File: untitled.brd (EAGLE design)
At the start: 59.4 x 57.8 mm, 21 parts

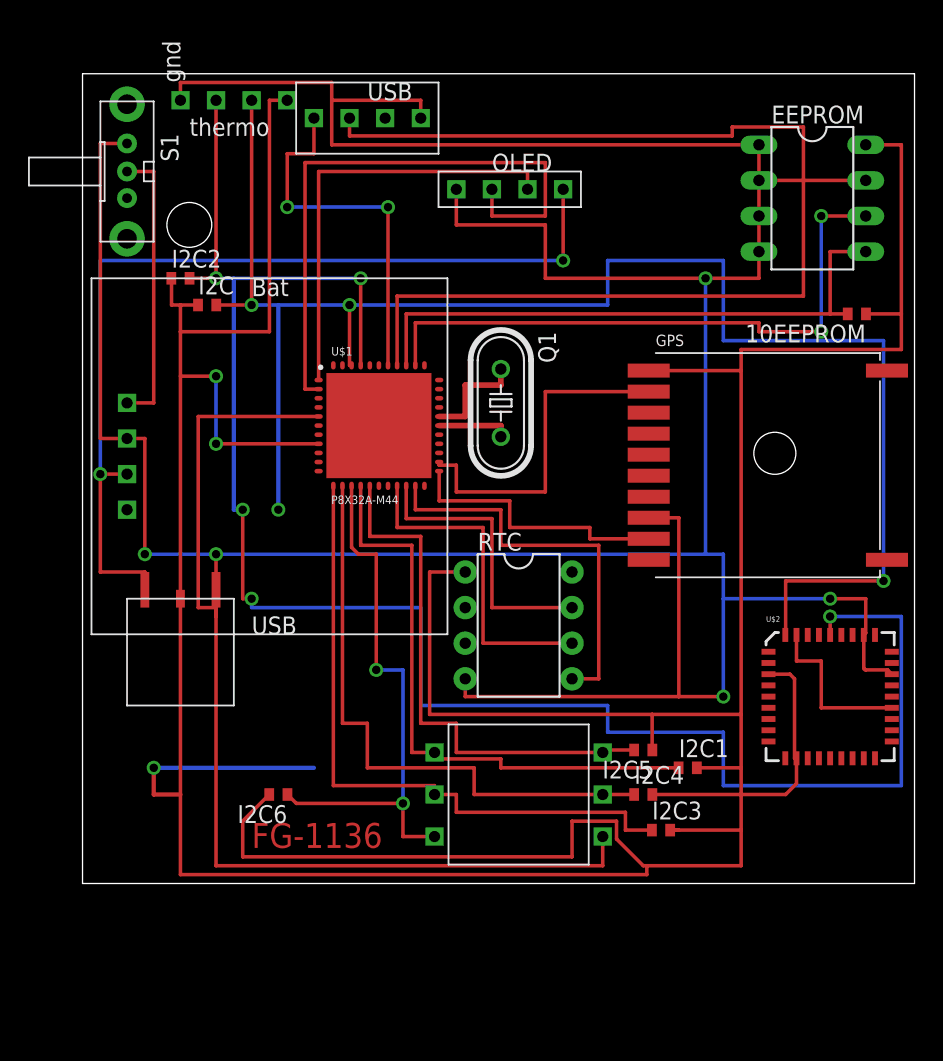
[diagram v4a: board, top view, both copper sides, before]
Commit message: Board cleanup
* Removed traces to nowhere
* Made all vias round
* Optimized some traces to remove vias
* Made better connections to SMT pads
* Connected missing ground on compass
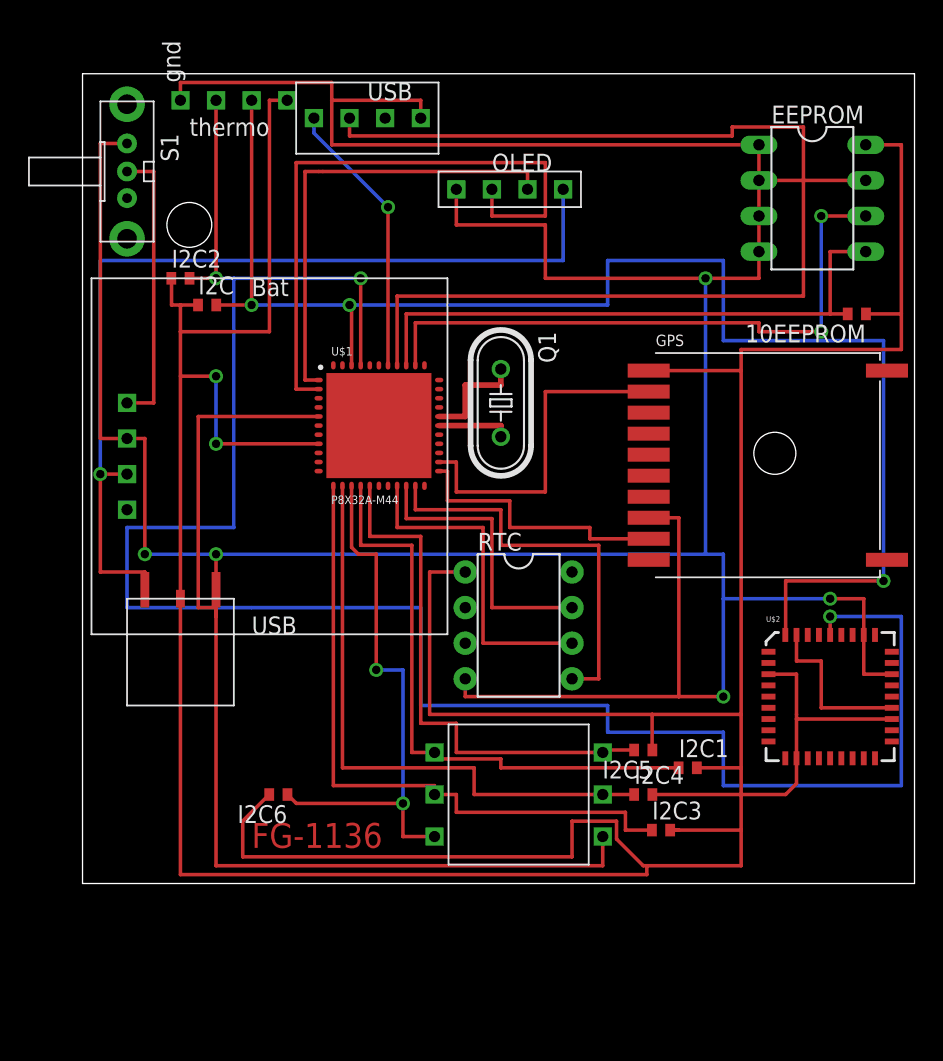
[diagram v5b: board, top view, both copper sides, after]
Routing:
- net SCL: track 133.4 -> 148.6 mm, vias 5 -> 3
- net SDA: track 118.2 -> 103.5 mm, vias 4 -> 3
- net VCC: track 303.6 -> 295.3 mm, vias 1 -> 0
- net N$7: track 26.7 -> 19.8 mm, vias 2 -> 1
- net N$11: track 31.1 -> 33.0 mm
- net N$10: track 43.8 -> 45.1 mm
- net N$12: vias 2 -> 1

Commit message: Add supply symbols, didn't fix board
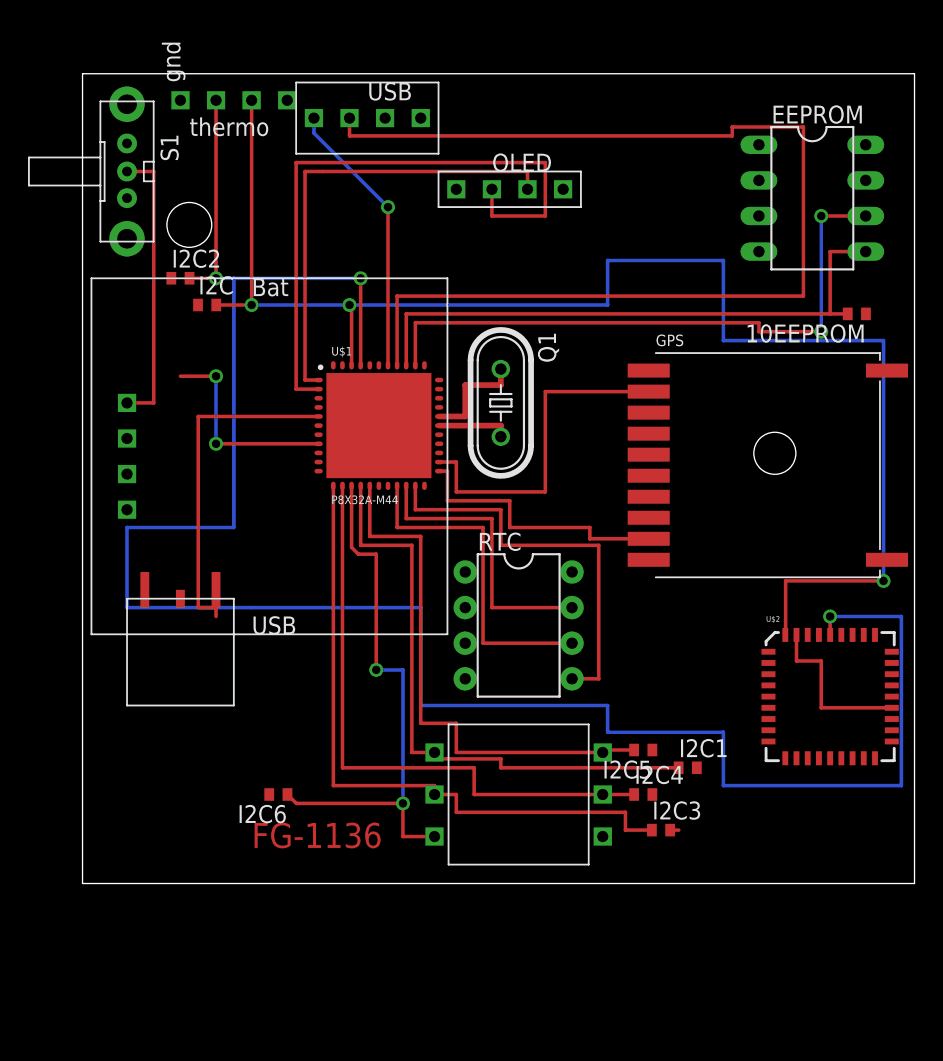
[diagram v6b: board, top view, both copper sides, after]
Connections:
- net N$12 renamed +5V
- removed net VCC: 10EEPROM.1, EEPROM.8, GPS.P$1, I2C.1, I2C1.2, I2C2.1, I2C3.2, I2C4.2, I2C5.1, I2C6.2, RTC.1, THERMO.VCC, U$2.11, U$2.21, U$2.3
- new net +3V3: 10EEPROM.1, 3.3LDO.VOUT, EEPROM.8, I2C.1, I2C1.2, I2C2.1, I2C3.2, I2C4.2, I2C5.1, I2C6.2, RTC.1, THERMO.VCC, U$2.11, U$2.21, U$2.3
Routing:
- net GND: track 309.1 -> 0.00 mm, vias 5 -> 0
- net VCC: track 295.3 -> 0.00 mm
- net +5V: track 66.0 -> 0.00 mm, vias 1 -> 0

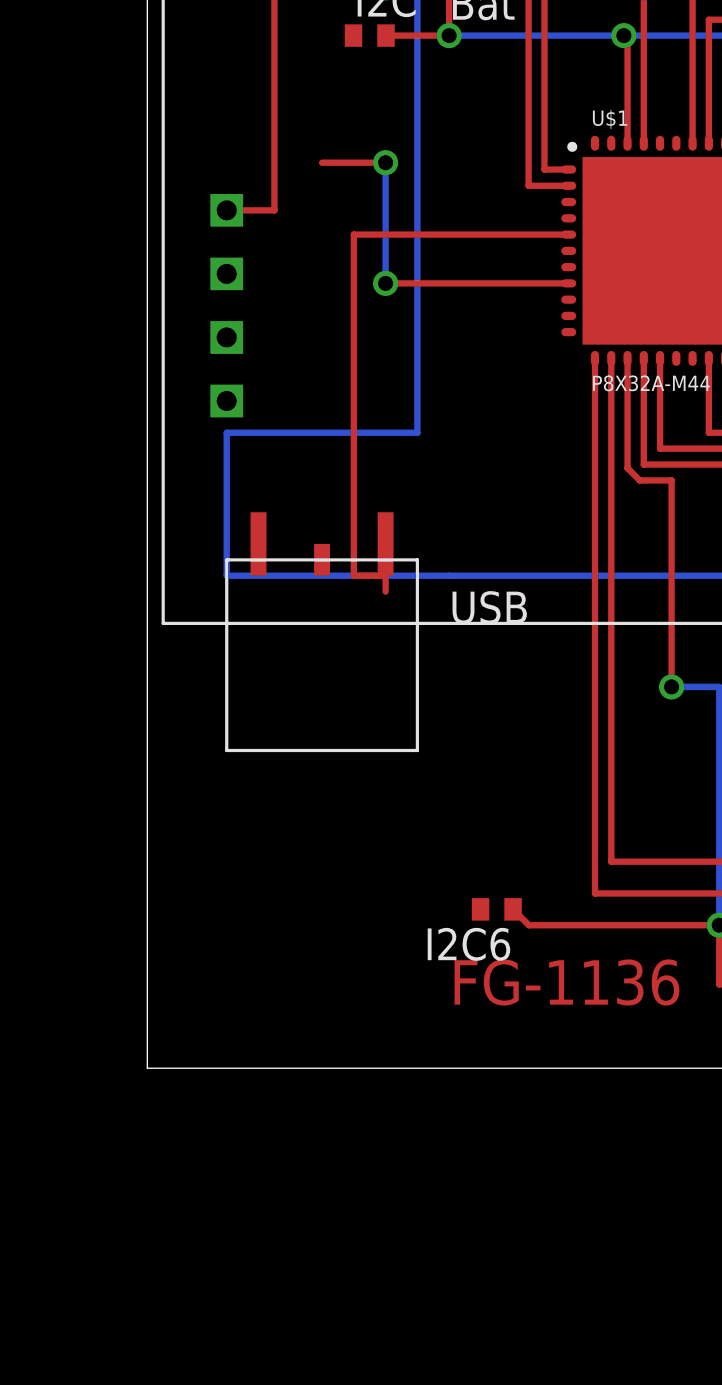
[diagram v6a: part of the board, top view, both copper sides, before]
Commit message: Added power and decoupling caps to schematic
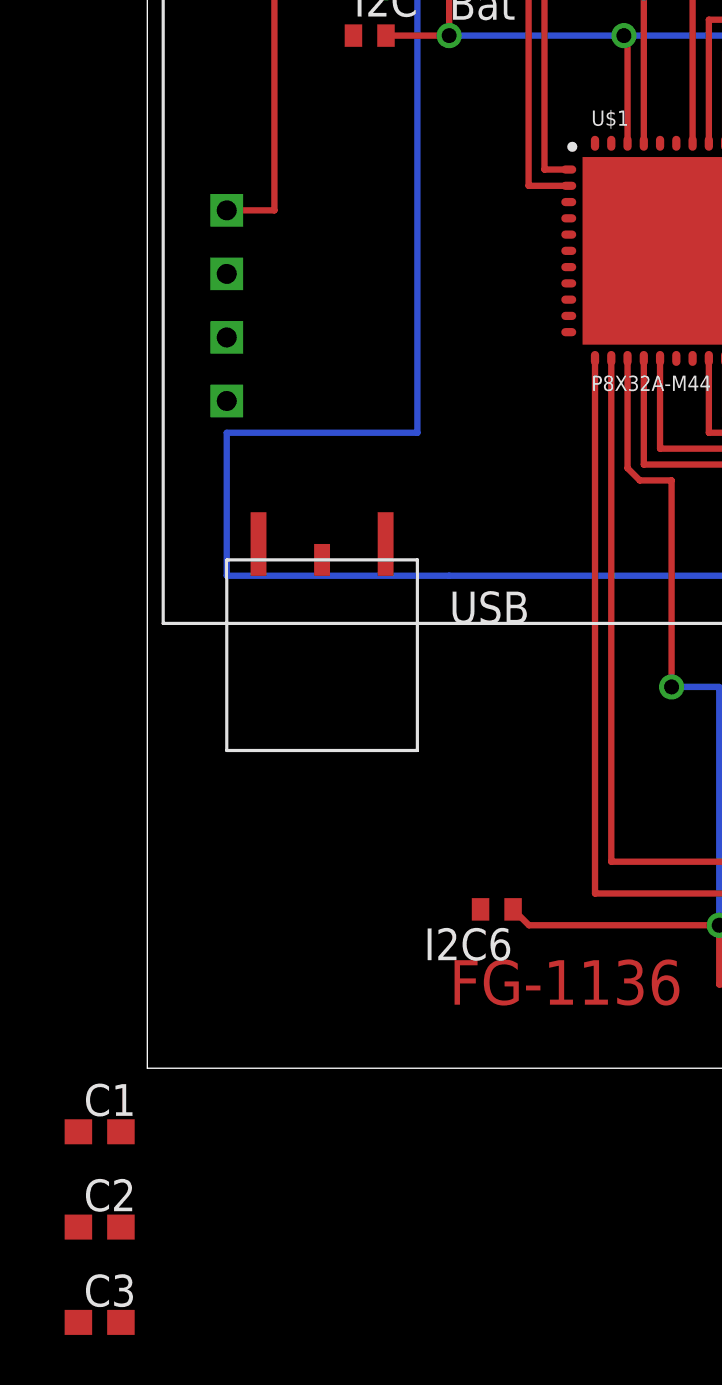
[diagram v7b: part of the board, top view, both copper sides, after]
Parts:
- added C1, C2, C3: (no value), rcl:C0603
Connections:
- removed net VDD: U$1.18, U$1.30, U$1.40, U$1.8
- removed net VSS: U$1.17, U$1.27, U$1.39, U$1.5
- net +3V3: now also C1.1, C2.1, C3.1, U$1.18, U$1.30, U$1.40, U$1.8
- net GND: now also C1.2, C2.2, C3.2, U$1.17, U$1.27, U$1.39, U$1.5
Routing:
- net VSS: track 24.1 -> 0.00 mm
- net VDD: track 14.7 -> 0.00 mm, vias 2 -> 0
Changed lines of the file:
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@@
 <element name="I2C1" library="adafruit" package="R1005" value="" x="76.835" y="18.415"/>
 <element name="U$2" library="SparkFun" package="LCC36" value="HMC6343A" x="86.995" y="23.495"/>
+<element name="C1" library="rcl" package="C0603" value="" x="31.75" y="7.62"/>
+<element name="C2" library="rcl" package="C0603" value="" x="31.75" y="3.81"/>
+<element name="C3" library="rcl" package="C0603" value="" x="31.75" y="0"/>
 </elements>
 <signals>
-<signal name="VDD">
-<contactref element="U$1" pad="8"/>
-<contactref element="U$1" pad="18"/>
-<contactref element="U$1" pad="30"/>
-<contactref element="U$1" pad="40"/>
-<wire x1="50.5" y1="41.5313" x2="43.18" y2="41.5313" width="0.254" layer="1"/>
-<wire x1="43.18" y1="41.5313" x2="43.18" y2="46.355" width="0.254" layer="16"/>
-<wire x1="43.18" y1="46.355" x2="40.64" y2="46.355" width="0.254" layer="1"/>
-<via x="43.18" y="41.5313" extent="1-16" drill="0.6"/>
-<via x="43.18" y="46.355" extent="1-16" drill="0.6"/>
-<wire x1="54.15" y1="47.1313" x2="59.1" y2="44.1313" width="0" layer="19" extent="1-1"/>
-<wire x1="55.45" y1="38.5313" x2="59.1" y2="44.1313" width="0" layer="19" extent="1-1"/>
-<wire x1="50.5" y1="41.5313" x2="55.45" y2="38.5313" width="0" layer="19" extent="1-1"/>
-</signal>
-<signal name="VSS">
-<contactref element="U$1" pad="5"/>
-<contactref element="U$1" pad="17"/>
-<contactref element="U$1" pad="27"/>
-<contactref element="U$1" pad="39"/>
-<wire x1="50.5" y1="43.4813" x2="41.91" y2="43.4813" width="0.254" layer="1"/>
-<wire x1="41.91" y1="43.4813" x2="41.91" y2="29.845" width="0.254" layer="1"/>
-<wire x1="41.91" y1="29.845" x2="43.18" y2="29.845" width="0.254" layer="1"/>
-<wire x1="43.18" y1="29.845" x2="43.18" y2="29.21" width="0.254" layer="1"/>
-<wire x1="54.8" y1="38.5313" x2="59.1" y2="42.1813" width="0" layer="19" extent="1-1"/>
-<wire x1="54.8" y1="47.1313" x2="59.1" y2="42.1813" width="0" layer="19" extent="1-1"/>
-<wire x1="50.5" y1="43.4813" x2="54.8" y2="47.1313" width="0" layer="19" extent="1-1"/>
-</signal>
 <signal name="VBAT">
 <contactref element="RTC" pad="8"/>
@@
 <contactref element="U$2" pad="29"/>
 <contactref element="THERMO" pad="GND"/>
+<contactref element="U$1" pad="39"/>
+<contactref element="U$1" pad="27"/>
+<contactref element="U$1" pad="17"/>
+<contactref element="U$1" pad="5"/>
+<contactref element="C2" pad="2"/>
+<contactref element="C1" pad="2"/>
+<contactref element="C3" pad="2"/>
 <wire x1="81.915" y1="60.325" x2="89.535" y2="60.325" width="0" layer="19" extent="1-1"/>
 <wire x1="81.915" y1="62.865" x2="81.915" y2="60.325" width="0" layer="19" extent="1-1"/>
@@
 <wire x1="81.915" y1="55.245" x2="81.915" y2="57.785" width="0" layer="19" extent="1-1"/>
 <wire x1="74.05" y1="36.255" x2="81.915" y2="55.245" width="0" layer="19" extent="1-1"/>
-<wire x1="60.96" y1="24.765" x2="74.05" y2="36.255" width="0" layer="19" extent="1-1"/>
+<wire x1="59.1" y1="42.1813" x2="74.05" y2="36.255" width="0" layer="19" extent="1-1"/>
+<wire x1="54.8" y1="38.5313" x2="59.1" y2="42.1813" width="0" layer="19" extent="1-1"/>
+<wire x1="54.8" y1="47.1313" x2="59.1" y2="42.1813" width="0" layer="19" extent="1-1"/>
+<wire x1="50.5" y1="43.4813" x2="54.8" y2="47.1313" width="0" layer="19" extent="1-1"/>
+<wire x1="43.18" y1="31.75" x2="54.8" y2="38.5313" width="0" layer="19" extent="1-1"/>
+<wire x1="36.83" y1="41.91" x2="43.18" y2="31.75" width="0" layer="19" extent="1-1"/>
+<wire x1="60.325" y1="59.69" x2="54.8" y2="47.1313" width="0" layer="19" extent="1-1"/>
+<wire x1="57.785" y1="64.77" x2="60.325" y2="59.69" width="0" layer="19" extent="1-1"/>
+<wire x1="60.96" y1="24.765" x2="54.8" y2="38.5313" width="0" layer="19" extent="1-1"/>
 <wire x1="70.77" y1="13.51" x2="60.96" y2="24.765" width="0" layer="19" extent="1-1"/>
+<wire x1="40.64" y1="66.04" x2="57.785" y2="64.77" width="0" layer="19" extent="1-1"/>
+<wire x1="36.83" y1="62.96" x2="40.64" y2="66.04" width="0" layer="19" extent="1-1"/>
 <wire x1="89.395" y1="27.895" x2="74.05" y2="36.255" width="0" layer="19" extent="1-1"/>
 <wire x1="91.395" y1="25.095" x2="89.395" y2="27.895" width="0" layer="19" extent="1-1"/>
-<wire x1="43.18" y1="31.75" x2="60.96" y2="24.765" width="0" layer="19" extent="1-1"/>
-<wire x1="36.83" y1="41.91" x2="43.18" y2="31.75" width="0" layer="19" extent="1-1"/>
-<wire x1="36.83" y1="62.96" x2="36.83" y2="41.91" width="0" layer="19" extent="1-1"/>
-<wire x1="40.64" y1="66.04" x2="36.83" y2="62.96" width="0" layer="19" extent="1-1"/>
-<wire x1="57.785" y1="64.77" x2="40.64" y2="66.04" width="0" layer="19" extent="1-1"/>
-<wire x1="60.325" y1="59.69" x2="57.785" y2="64.77" width="0" layer="19" extent="1-1"/>
+<wire x1="32.6" y1="7.62" x2="43.18" y2="31.75" width="0" layer="19" extent="1-1"/>
+<wire x1="32.6" y1="3.81" x2="32.6" y2="7.62" width="0" layer="19" extent="1-1"/>
+<wire x1="32.6" y1="0" x2="32.6" y2="3.81" width="0" layer="19" extent="1-1"/>
 </signal>
 <signal name="+5V">
@@
 <contactref element="10EEPROM" pad="1"/>
 <contactref element="I2C" pad="1"/>
+<contactref element="U$1" pad="8"/>
+<contactref element="U$1" pad="18"/>
+<contactref element="U$1" pad="30"/>
+<contactref element="U$1" pad="40"/>
+<contactref element="C1" pad="1"/>
+<contactref element="C2" pad="1"/>
+<contactref element="C3" pad="1"/>
 <wire x1="89.55" y1="50.8" x2="89.535" y2="62.865" width="0" layer="19" extent="1-1"/>
 <wire x1="82.595" y1="25.095" x2="89.55" y2="50.8" width="0" layer="19" extent="1-1"/>
@@
 <wire x1="91.395" y1="21.895" x2="84.595" y2="19.095" width="0" layer="19" extent="1-1"/>
 <wire x1="60.96" y1="32.385" x2="74.31" y2="19.685" width="0" layer="19" extent="1-1"/>
-<wire x1="40.64" y1="30.48" x2="60.96" y2="32.385" width="0" layer="19" extent="1-1"/>
+<wire x1="55.45" y1="38.5313" x2="60.96" y2="32.385" width="0" layer="19" extent="1-1"/>
+<wire x1="50.5" y1="41.5313" x2="55.45" y2="38.5313" width="0" layer="19" extent="1-1"/>
+<wire x1="59.1" y1="44.1313" x2="55.45" y2="38.5313" width="0" layer="19" extent="1-1"/>
+<wire x1="54.15" y1="47.1313" x2="59.1" y2="44.1313" width="0" layer="19" extent="1-1"/>
+<wire x1="41.895" y1="51.435" x2="54.15" y2="47.1313" width="0" layer="19" extent="1-1"/>
+<wire x1="39.99" y1="53.34" x2="41.895" y2="51.435" width="0" layer="19" extent="1-1"/>
+<wire x1="40.64" y1="30.48" x2="50.5" y2="41.5313" width="0" layer="19" extent="1-1"/>
+<wire x1="48.26" y1="66.04" x2="39.99" y2="53.34" width="0" layer="19" extent="1-1"/>
 <wire x1="46.975" y1="16.51" x2="40.64" y2="30.48" width="0" layer="19" extent="1-1"/>
-<wire x1="41.895" y1="51.435" x2="40.64" y2="30.48" width="0" layer="19" extent="1-1"/>
-<wire x1="39.99" y1="53.34" x2="41.895" y2="51.435" width="0" layer="19" extent="1-1"/>
-<wire x1="48.26" y1="66.04" x2="39.99" y2="53.34" width="0" layer="19" extent="1-1"/>
+<wire x1="30.9" y1="7.62" x2="46.975" y2="16.51" width="0" layer="19" extent="1-1"/>
+<wire x1="30.9" y1="3.81" x2="30.9" y2="7.62" width="0" layer="19" extent="1-1"/>
+<wire x1="30.9" y1="0" x2="30.9" y2="3.81" width="0" layer="19" extent="1-1"/>
 </signal>
 </signals>

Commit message: Connected BOEn to GND
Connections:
- net GND: now also U$1.6
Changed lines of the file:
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@@
 <contactref element="C1" pad="2"/>
 <contactref element="C3" pad="2"/>
+<contactref element="U$1" pad="6"/>
 <wire x1="81.915" y1="60.325" x2="89.535" y2="60.325" width="0" layer="19" extent="1-1"/>
 <wire x1="81.915" y1="62.865" x2="81.915" y2="60.325" width="0" layer="19" extent="1-1"/>
@@
 <wire x1="59.1" y1="42.1813" x2="74.05" y2="36.255" width="0" layer="19" extent="1-1"/>
 <wire x1="54.8" y1="38.5313" x2="59.1" y2="42.1813" width="0" layer="19" extent="1-1"/>
-<wire x1="54.8" y1="47.1313" x2="59.1" y2="42.1813" width="0" layer="19" extent="1-1"/>
-<wire x1="50.5" y1="43.4813" x2="54.8" y2="47.1313" width="0" layer="19" extent="1-1"/>
-<wire x1="43.18" y1="31.75" x2="54.8" y2="38.5313" width="0" layer="19" extent="1-1"/>
+<wire x1="50.5" y1="42.8313" x2="54.8" y2="38.5313" width="0" layer="19" extent="1-1"/>
+<wire x1="50.5" y1="43.4813" x2="50.5" y2="42.8313" width="0" layer="19" extent="1-1"/>
+<wire x1="54.8" y1="47.1313" x2="50.5" y2="43.4813" width="0" layer="19" extent="1-1"/>
+<wire x1="43.18" y1="31.75" x2="50.5" y2="42.8313" width="0" layer="19" extent="1-1"/>
 <wire x1="36.83" y1="41.91" x2="43.18" y2="31.75" width="0" layer="19" extent="1-1"/>
 <wire x1="60.325" y1="59.69" x2="54.8" y2="47.1313" width="0" layer="19" extent="1-1"/>
